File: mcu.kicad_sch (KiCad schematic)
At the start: 22 parts, among them J1 SWD_DBG, U1 STM32F405RGTx, Y1 8MHz

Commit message: audio part
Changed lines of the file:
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@@
+	(wire
+		(pts
+			(xy 161.29 57.15) (xy 165.1 57.15)
+		)
+		(stroke
+			(width 0)
+			(type default)
+		)
+	)
 	(wire
 		(pts
@@
 		(pts
 			(xy 187.96 105.41) (xy 187.96 106.68)
-		)
-		(stroke
-			(width 0)
-			(type default)
-		)
-	)
-	(wire
-		(pts
-			(xy 165.1 57.15) (xy 161.29 57.15)
 		)
 		(stroke
@@
 	(hierarchical_label "PTT_OUT"
 		(shape output)
-		(at 236.22 115.57 180)
-		(fields_autoplaced yes)
-		(effects
-			(font
-				(size 1.27 1.27)
-			)
-			(justify right)
+		(at 227.33 115.57 0)
+		(fields_autoplaced yes)
+		(effects
+			(font
+				(size 1.27 1.27)
+			)
+			(justify left)
 		)
 	)
@@
 	(hierarchical_label "RF_PWR"
 		(shape output)
-		(at 236.22 120.65 180)
-		(fields_autoplaced yes)
-		(effects
-			(font
-				(size 1.27 1.27)
-			)
-			(justify right)
+		(at 227.33 120.65 0)
+		(fields_autoplaced yes)
+		(effects
+			(font
+				(size 1.27 1.27)
+			)
+			(justify left)
 		)
 	)
@@
 		)
 	)
-	(hierarchical_label "RF_ENA"
-		(shape output)
-		(at 236.22 118.11 180)
-		(fields_autoplaced yes)
-		(effects
-			(font
-				(size 1.27 1.27)
-			)
-			(justify right)
+	(hierarchical_label "~{RF_ENA}"
+		(shape output)
+		(at 227.33 118.11 0)
+		(fields_autoplaced yes)
+		(effects
+			(font
+				(size 1.27 1.27)
+			)
+			(justify left)
 		)
 	)
@@
 		)
 	)
+	(hierarchical_label "AF_AMP_EN"
+		(shape output)
+		(at 227.33 128.27 0)
+		(fields_autoplaced yes)
+		(effects
+			(font
+				(size 1.27 1.27)
+			)
+			(justify left)
+		)
+	)
 	(hierarchical_label "KEY_ROWS"
 		(shape input)
@@
 		)
 	)
+	(hierarchical_label "VIBR"
+		(shape output)
+		(at 227.33 125.73 0)
+		(fields_autoplaced yes)
+		(effects
+			(font
+				(size 1.27 1.27)
+			)
+			(justify left)
+		)
+	)
 	(hierarchical_label "PWM_BLIGHT"
 		(shape output)
-		(at 236.22 123.19 180)
-		(fields_autoplaced yes)
-		(effects
-			(font
-				(size 1.27 1.27)
-			)
-			(justify right)
-		)
-	)
+		(at 227.33 123.19 0)
+		(fields_autoplaced yes)
+		(effects
+			(font
+				(size 1.27 1.27)
+			)
+			(justify left)
+		)
+	)

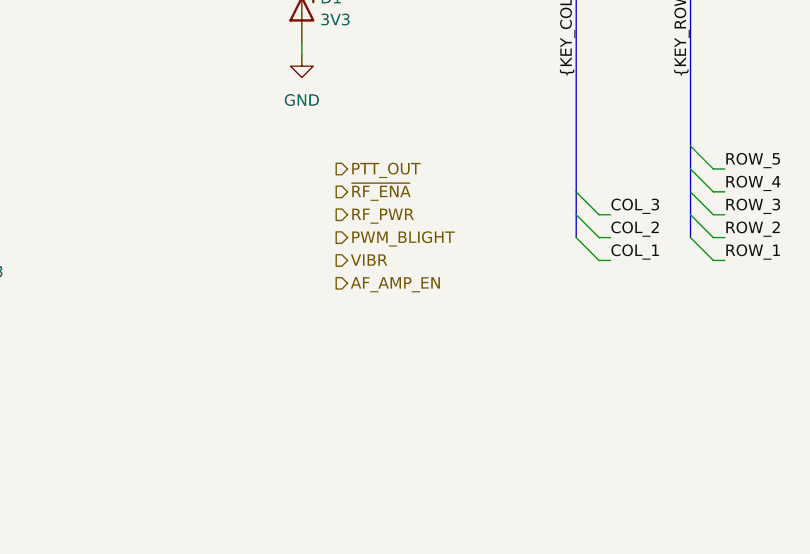
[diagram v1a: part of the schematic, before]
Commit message: spk/mic update
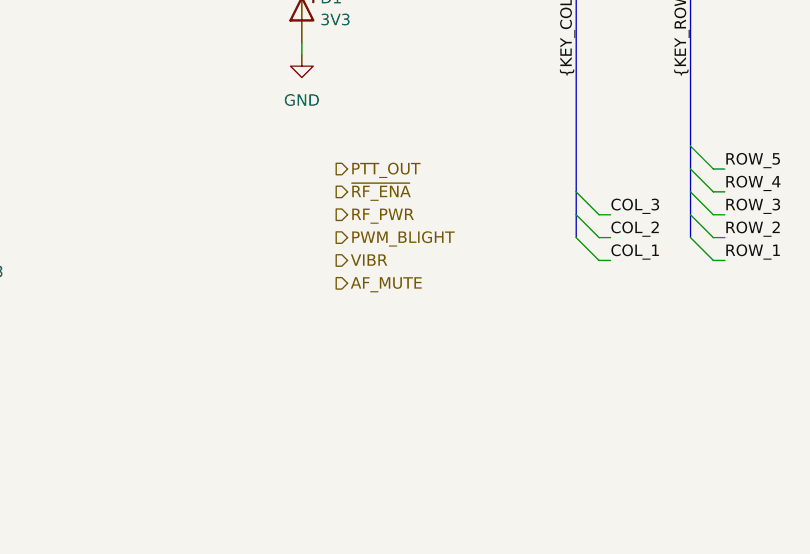
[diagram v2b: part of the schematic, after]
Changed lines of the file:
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@@
 	(title_block
 		(title "Mainboard replacement for Nokia 3310")
-		(date "25-10-2024")
+		(date "28-10-2024")
 		(rev "Rev A")
 		(company "M17 Project")
@@
 		)
 	)
-	(hierarchical_label "AF_AMP_EN"
+	(hierarchical_label "AF_MUTE"
 		(shape output)
 		(at 227.33 128.27 0)

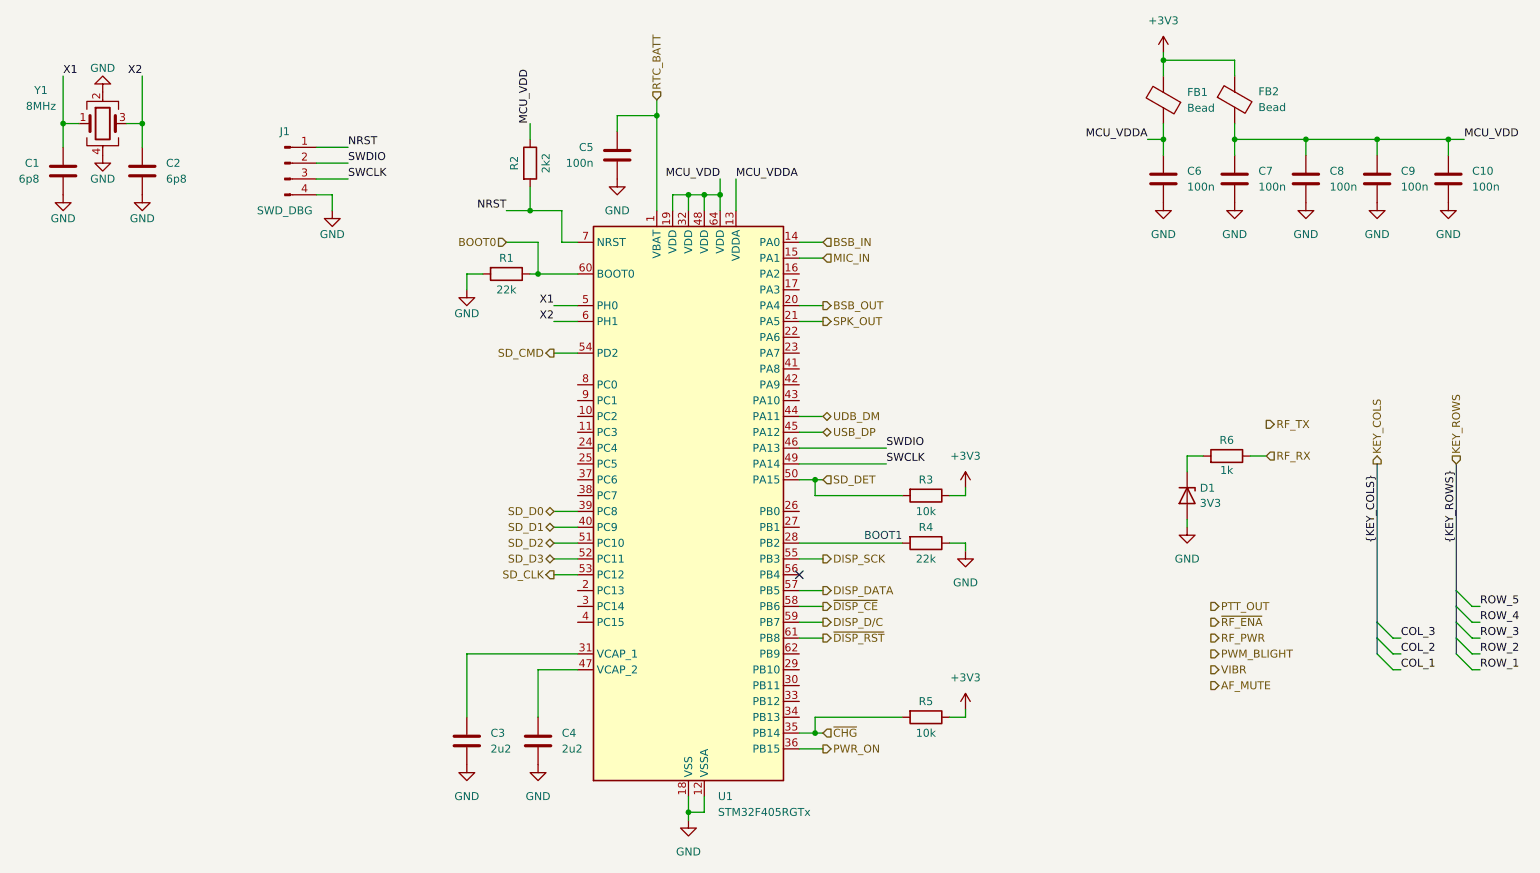
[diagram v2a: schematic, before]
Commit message: removed audio part
- added buzzer
- added battery voltage measurement
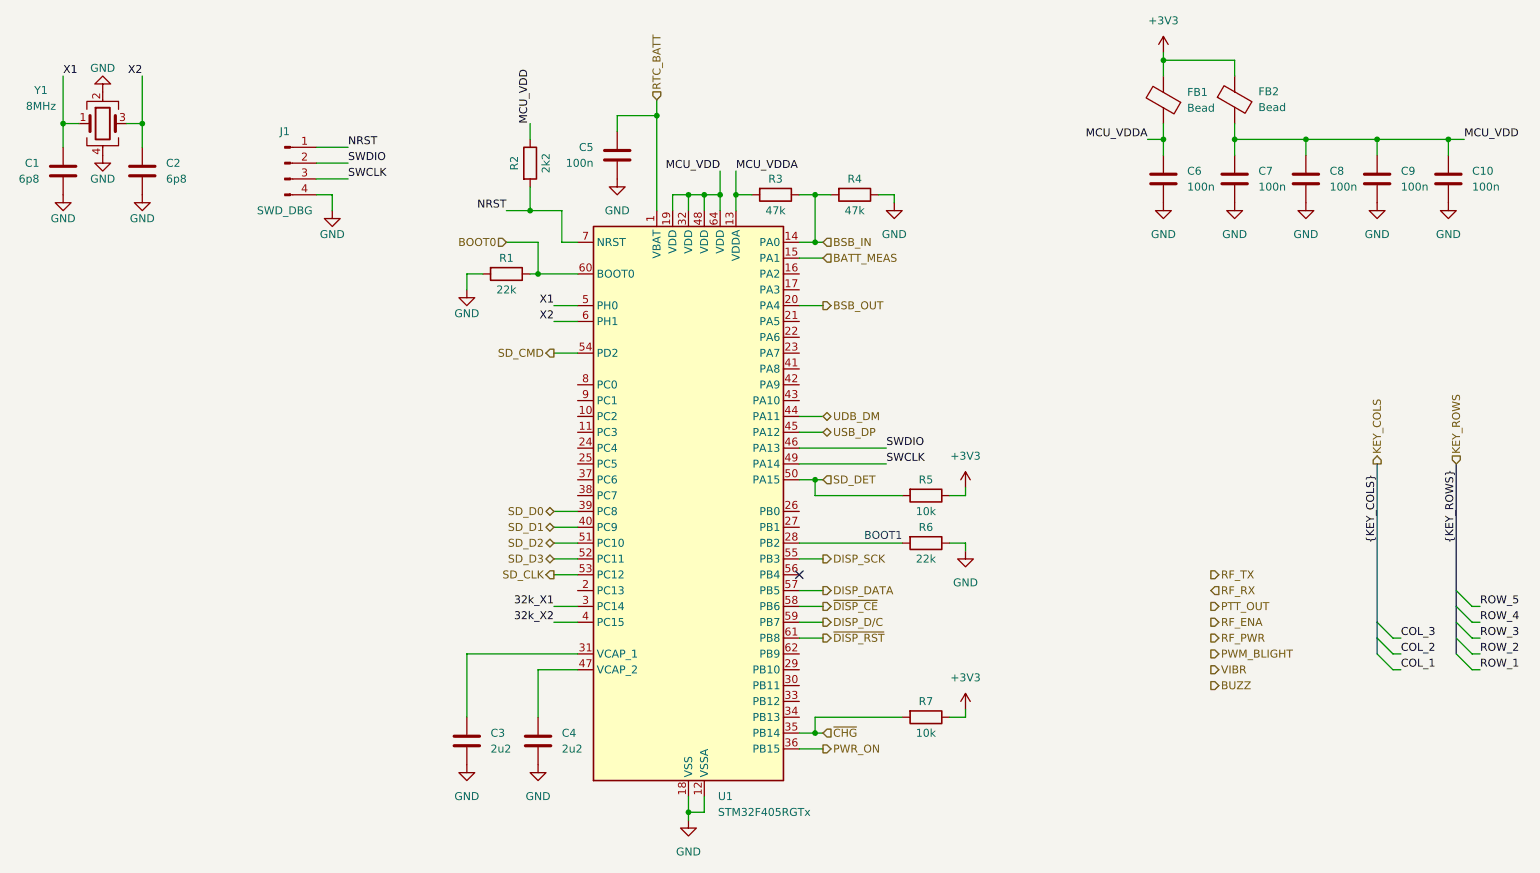
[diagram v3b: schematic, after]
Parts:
- removed D1: 3V3, symbol Device:D_Zener
- removed R6: 1k, Inductor_SMD:L_0805_2012Metric, symbol Device:R
- added R3, R4: 47k, Inductor_SMD:L_0805_2012Metric, symbol Device:R
- renumbered R3 to R5, R4 to R6, R5 to R7
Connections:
- net BSB_IN: now also R3.1, R4.2
- net GND: now also R4.1
- net MCU_VDDA: now also R3.2
- net 32k_X1: now reaches U1.3 (PC14)
- net 32k_X2: now reaches U1.4 (PC15)
- net MIC_IN renamed BATT_MEAS
- net SPK_OUT: no longer names the net of U1.21 (PA5)

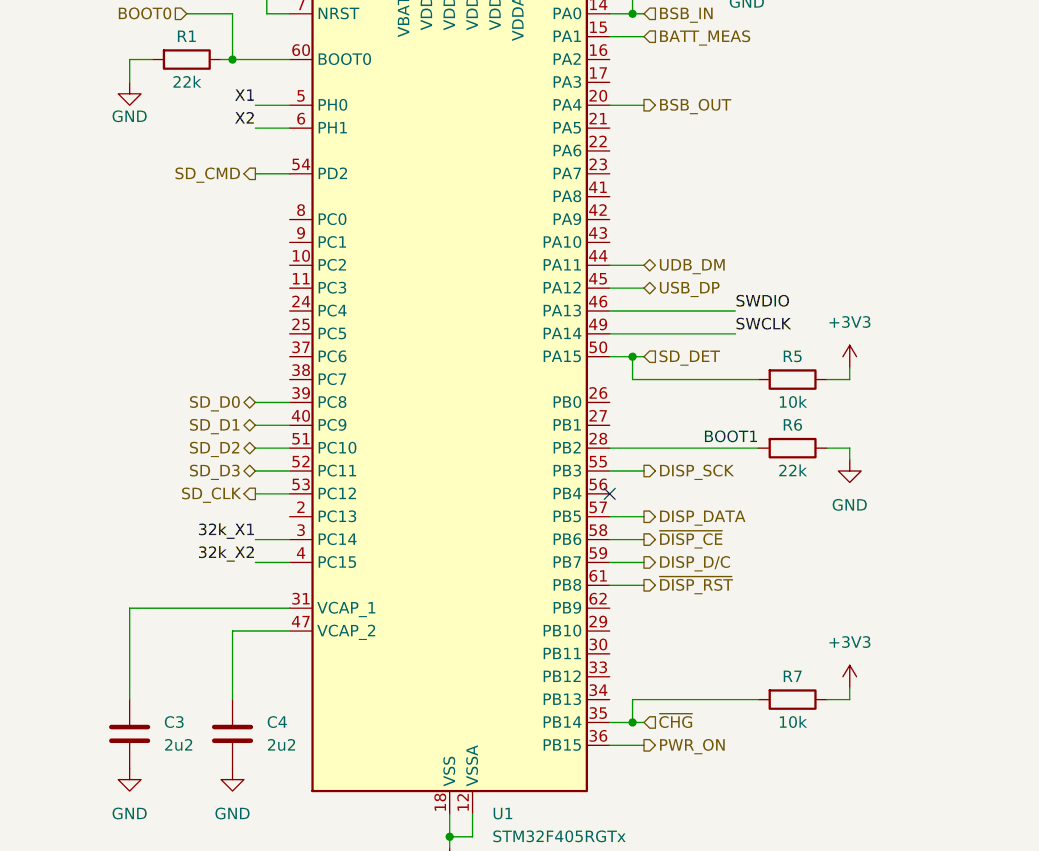
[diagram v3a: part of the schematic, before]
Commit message: mayhem
- removed sd card slot
- started pcb design
- added nice 3310 photos
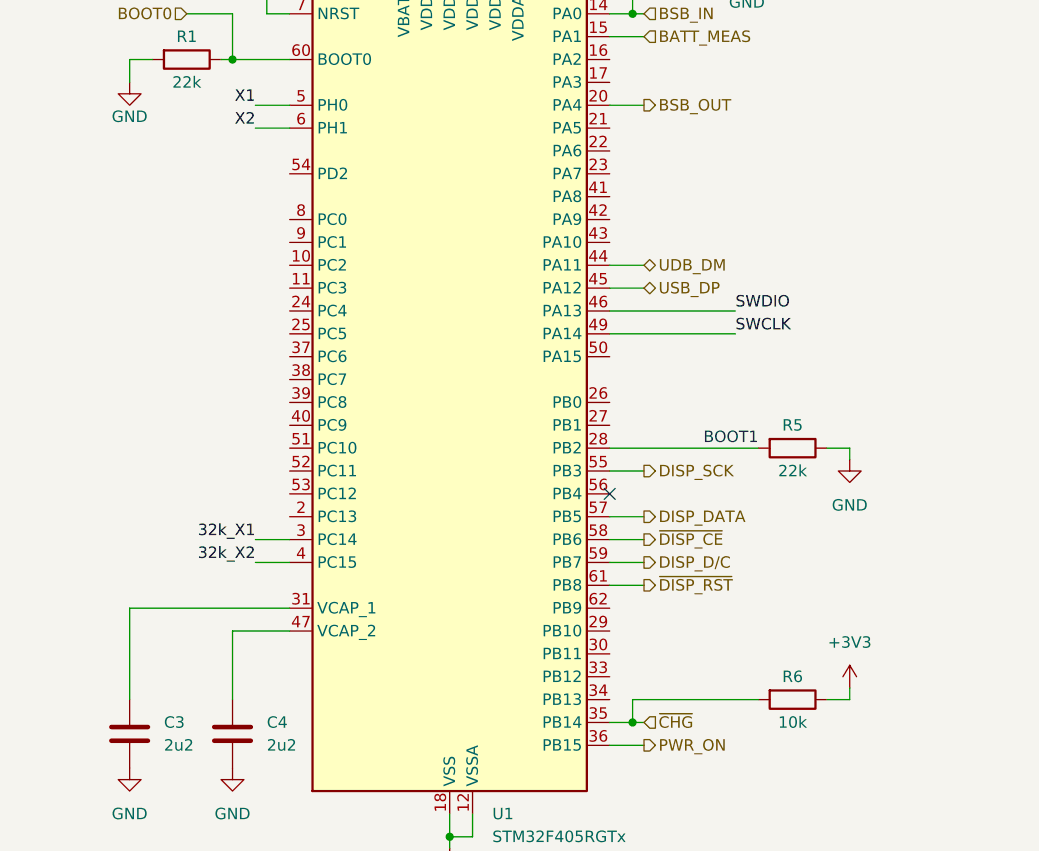
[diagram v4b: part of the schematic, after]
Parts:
- removed R5: 10k, Inductor_SMD:L_0805_2012Metric, symbol Device:R
- J1: footprint (none) -> Parts:3310_4_pin
- renumbered R6 to R5, R7 to R6
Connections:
- net SD_CLK: no longer names the net of U1.53 (PC12)
- net SD_CMD: no longer names the net of U1.54 (PD2)
- net SD_D0: no longer names the net of U1.39 (PC8)
- net SD_D1: no longer names the net of U1.40 (PC9)
- net SD_D2: no longer names the net of U1.51 (PC10)
- net SD_D3: no longer names the net of U1.52 (PC11)
- net SD_DET: no longer names the net of U1.50 (PA15)

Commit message: pcb update
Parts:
- C1, C2: footprint (none) -> Capacitor_SMD:C_0805_2012Metric
- R1, R2, R3, R4, R5, R6: footprint Inductor_SMD:L_0805_2012Metric -> Resistor_SMD:R_0805_2012Metric
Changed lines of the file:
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@@
 	(title_block
 		(title "Mainboard replacement for Nokia 3310")
-		(date "31-10-2024")
+		(date "2-11-2024")
 		(rev "Rev A")
 		(company "M17 Project")
@@
 			)
 		)
-		(property "Footprint" "Inductor_SMD:L_0805_2012Metric"
+		(property "Footprint" "Resistor_SMD:R_0805_2012Metric"
 			(at 114.3 60.452 90)
 			(effects
@@
 			)
 		)
-		(property "Footprint" ""
+		(property "Footprint" "Capacitor_SMD:C_0805_2012Metric"
 			(at 56.8452 49.53 0)
 			(effects
@@
 			)
 		)
-		(property "Footprint" "Inductor_SMD:L_0805_2012Metric"
+		(property "Footprint" "Resistor_SMD:R_0805_2012Metric"
 			(at 181.61 131.572 90)
 			(effects
@@
 			)
 		)
-		(property "Footprint" "Inductor_SMD:L_0805_2012Metric"
+		(property "Footprint" "Resistor_SMD:R_0805_2012Metric"
 			(at 170.18 47.752 90)
 			(effects
@@
 			)
 		)
-		(property "Footprint" "Inductor_SMD:L_0805_2012Metric"
+		(property "Footprint" "Resistor_SMD:R_0805_2012Metric"
 			(at 157.48 47.752 90)
 			(effects
@@
 			)
 		)
-		(property "Footprint" "Inductor_SMD:L_0805_2012Metric"
+		(property "Footprint" "Resistor_SMD:R_0805_2012Metric"
 			(at 116.332 44.45 90)
 			(effects
@@
 			)
 		)
-		(property "Footprint" ""
+		(property "Footprint" "Capacitor_SMD:C_0805_2012Metric"
 			(at 42.2148 49.53 0)
 			(effects
@@
 			)
 		)
-		(property "Footprint" "Inductor_SMD:L_0805_2012Metric"
+		(property "Footprint" "Resistor_SMD:R_0805_2012Metric"
 			(at 181.61 103.632 90)
 			(effects

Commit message: more pcb routing
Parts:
- C1, C10, C2, C3, C4, C5, C6, C7, C8, C9: footprint Capacitor_SMD:C_0805_2012Metric -> Capacitor_SMD:C_0402_1005Metric
- R1, R2, R3, R4, R5, R6: footprint Resistor_SMD:R_0805_2012Metric -> Resistor_SMD:R_0402_1005Metric
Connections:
- net BUZZ: now also U1.34 (PB13)
- net PTT_OUT: now also U1.8 (PC0)
- net PWM_BLIGHT: now also U1.16 (PA2)
- net RF_ENA: now also U1.62 (PB9)
- net RF_PWR: now also U1.2 (PC13)
- net RF_RX: now also U1.52 (PC11)
- net RF_TX: now also U1.51 (PC10)
- net VIBR: now also U1.17 (PA3)
- net X1: now also C2.1, Y1.3; no longer C1.1, Y1.1
- net X2: now also C1.1, Y1.1; no longer C2.1, Y1.3
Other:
- moved on the sheet: R6
